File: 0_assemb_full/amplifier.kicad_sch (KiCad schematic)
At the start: 4 parts

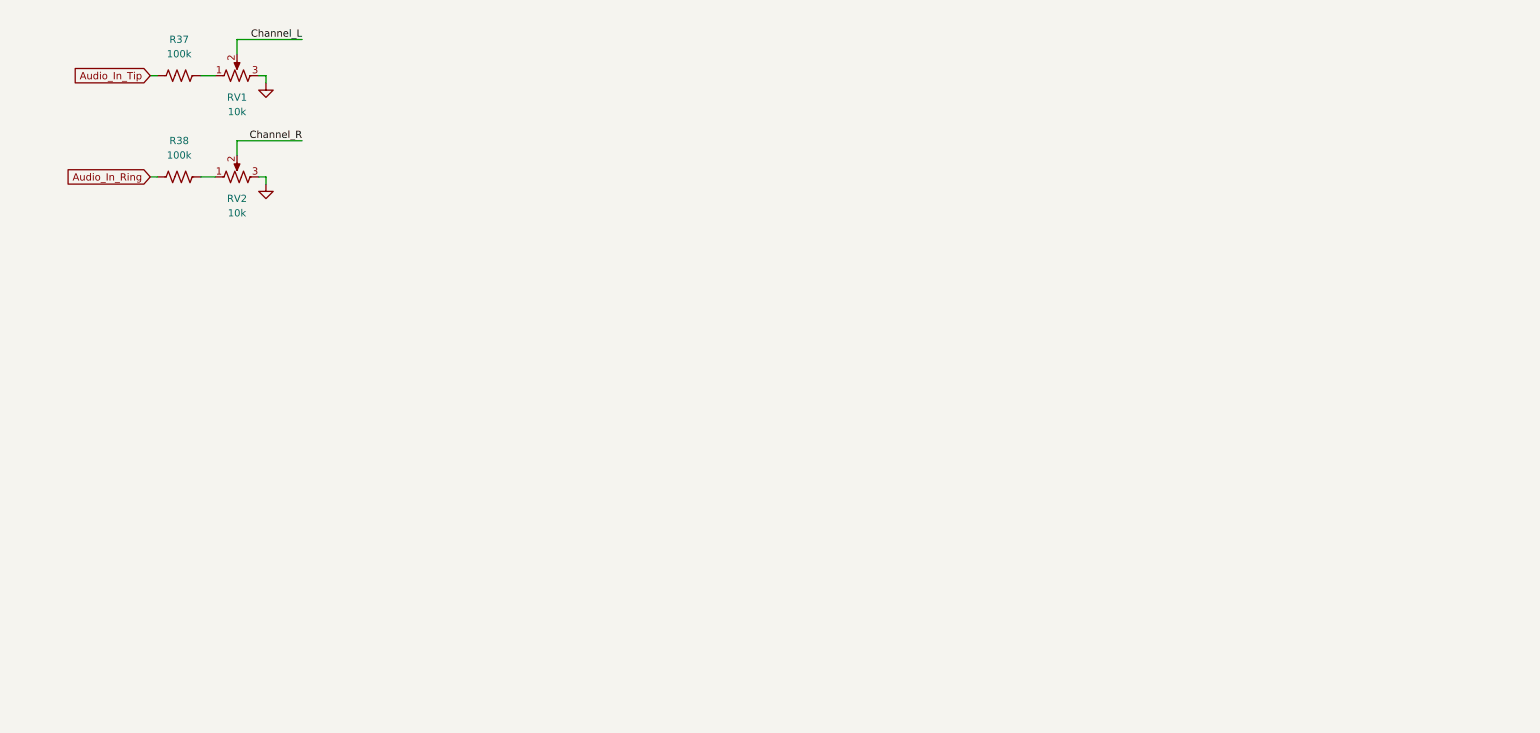
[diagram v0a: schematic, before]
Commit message: Added amplifier circuit and the programming header.
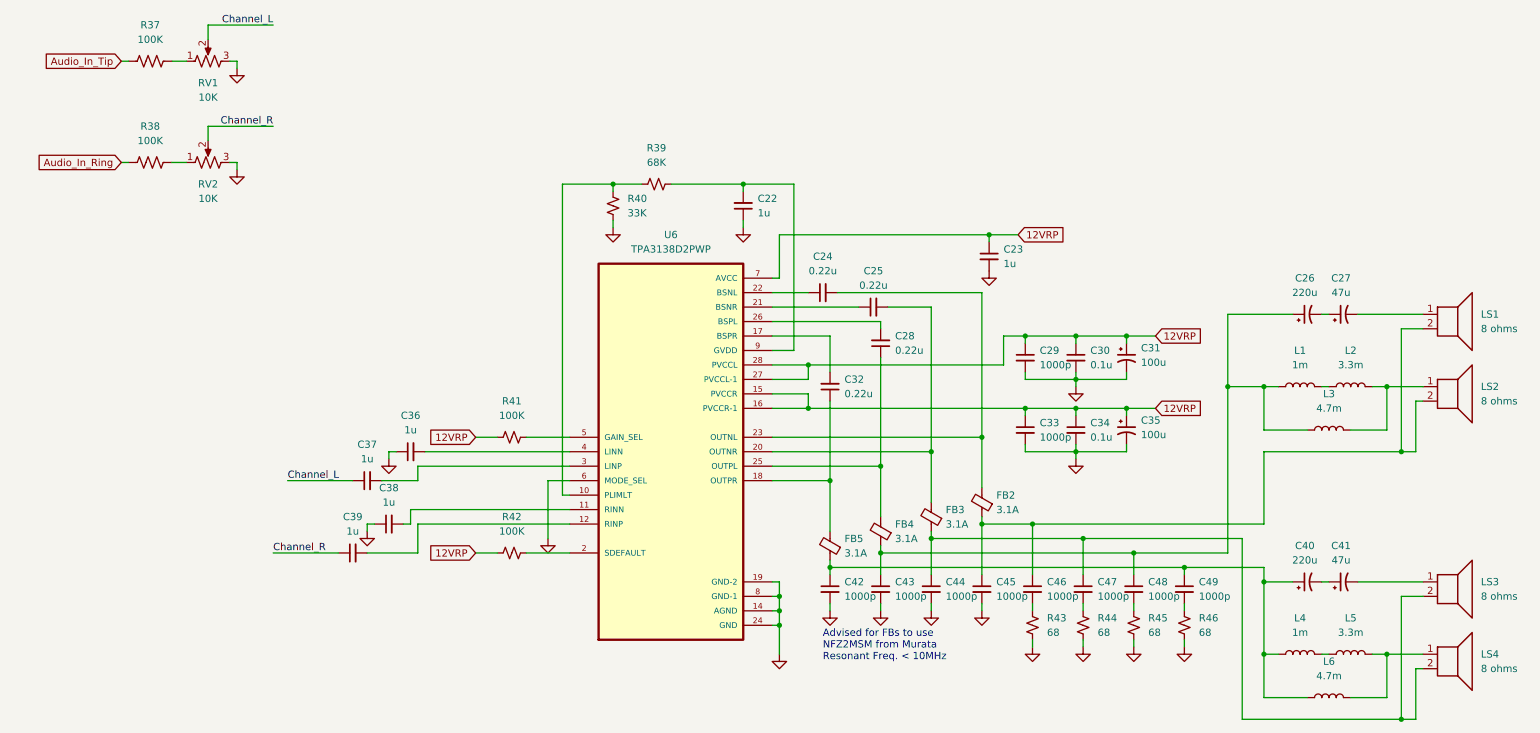
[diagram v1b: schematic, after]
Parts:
- added C22, C23, C36, C37, C38, C39: 1u, symbol Device:C_Small
- added C24, C25, C28, C32: 0.22u, symbol Device:C_Small
- added C26, C40: 220u, symbol Device:C_Polarized_Small_US
- added C27, C41: 47u, symbol Device:C_Polarized_Small_US
- added C29, C33, C42, C43, C44, C45, C46, C47, C48, C49: 1000p, symbol Device:C_Small
- added C30, C34: 0.1u, symbol Device:C_Small
- added C31, C35: 100u, symbol Device:C_Polarized_Small_US
- added FB2, FB3, FB4, FB5: 3.1A, symbol Device:FerriteBead_Small
- added L1, L4: 1m, symbol Device:L
- added L2, L5: 3.3m, symbol Device:L
- added L3, L6: 4.7m, symbol Device:L
- added LS1, LS2, LS3, LS4: 8 ohms, symbol Device:Speaker
- added R39: 68K, symbol Device:R_Small_US
- added R40: 33K, symbol Device:R_Small_US
- added R41, R42: 100K, symbol Device:R_Small_US
- added R43, R44, R45, R46: 68, symbol Device:R_Small_US
- added U6: TPA3138D2PWP, TPA3138D2PWP:IC_TPS61196PWPRQ1, symbol Specifics:TPA3138D2PWP
- R37, R38: value 100k -> 100K
- RV1, RV2: value 10k -> 10K
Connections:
- net Channel_L: now also C37.1
- net Channel_R: now also C39.1
- net GND: now also C22.1, C23.2, C29.2, C30.2, C31.2, C33.2, C34.2, C35.2, C36.1, C38.1, C42.2, C43.2, C44.2, C45.2, R40.1, R43.1, R44.1, R45.1, R46.1, U6.14 (AGND), U6.19 (GND-2), U6.24 (GND), U6.6 (MODE_SEL), U6.8 (GND-1)
- new net: R41.2, U6.5 (GAIN_SEL)
- new net: C26.1, C43.1, C48.1, FB4.1, L1.1, L3.1
- new net: L1.2, L2.1
- new net: L5.2, L6.2, LS4.1
- new net: C44.1, C47.1, FB3.1, LS3.2, LS4.2
- new net: C49.2, R46.2
- new net: C24.1, U6.22 (BSNL)
- new net: C24.2, FB2.2, U6.23 (OUTNL)
- new net: C26.2, C27.1
- new net: C27.2, LS1.1
- new net: R39.1, R40.2, U6.10 (PLIMLT)
- new net: C45.1, C46.1, FB2.1, LS1.2, LS2.2
- new net: C32.1, FB5.2, U6.18 (OUTPR)
- new net: C32.2, U6.17 (BSPR)
- new net: C46.2, R43.2
- new net: L2.2, L3.2, LS2.1
- new net: C47.2, R44.2
- new net: C28.1, FB4.2, U6.25 (OUTPL)
- new net: C36.2, U6.4 (LINN)
- new net: C38.2, U6.11 (RINN)
- new net: C25.2, FB3.2, U6.20 (OUTNR)
- new net: C40.1, C42.1, C49.1, FB5.1, L4.1, L6.1
- new net: C40.2, C41.1
- new net: C28.2, U6.26 (BSPL)
- new net: C37.2, U6.3 (LINP)
- new net: C48.2, R45.2
- new net: C41.2, LS3.1
- new net: C39.2, U6.12 (RINP)
- new net: R42.2, U6.2 (SDEFAULT)
- new net: C25.1, U6.21 (BSNR)
- new net: C22.2, R39.2, U6.9 (GVDD)
- new net: L4.2, L5.1
- new net 12VRP: C23.1, C29.1, C30.1, C31.1, C33.1, C34.1, C35.1, R41.1, R42.1, U6.15 (PVCCR), U6.16 (PVCCR-1), U6.27 (PVCCL-1), U6.28 (PVCCL), U6.7 (AVCC)
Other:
- note added: "Advised for FBs to use NFZ2MSM from Murata Resonant Freq. < 10MHz"
- moved on the sheet: R37, R38, RV1, RV2

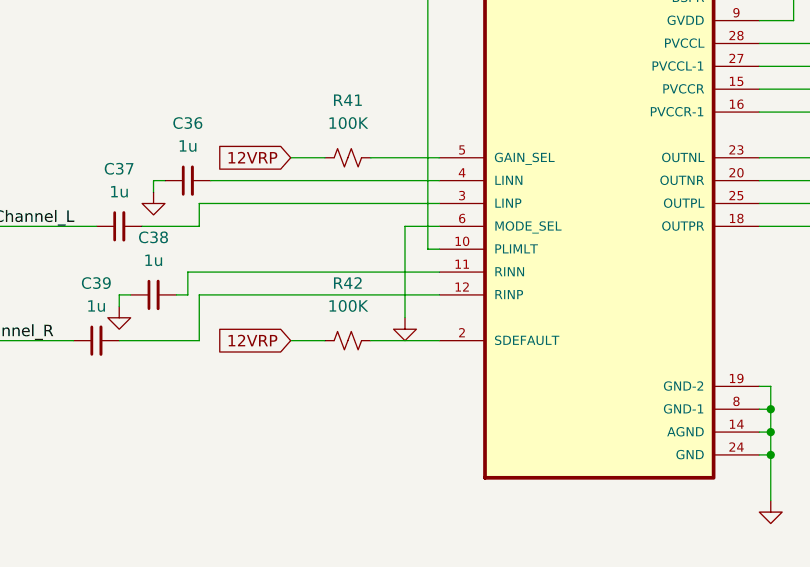
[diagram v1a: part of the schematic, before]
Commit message: A lot of work done on the STM32 PCB layout.
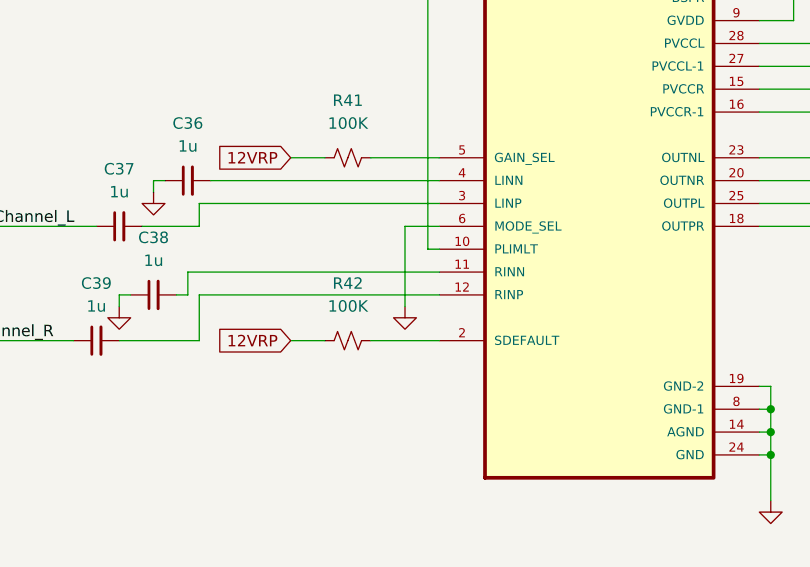
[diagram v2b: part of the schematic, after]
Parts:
- C22, C23, C31, C35, C36, C37, C38, C39: footprint (none) -> Capacitor_THT:CP_Radial_D5.0mm_P2.50mm
- C24, C25, C28, C29, C30, C32, C33, C34, C42, C43, C44, C45, C46, C47, C48, C49: footprint (none) -> Capacitor_SMD:C_0805_2012Metric_Pad1.18x1.45mm_HandSolder
- C26, C27, C40, C41: footprint (none) -> Capacitor_THT:CP_Radial_D6.3mm_P2.50mm
- FB2, FB3, FB4, FB5: footprint (none) -> Specifics:BEADC2016X100N
- L1, L2, L3, L4, L5, L6: footprint (none) -> Inductor_THT:L_Radial_D9.5mm_P5.00mm_Fastron_07HVP
- LS1, LS2, LS3, LS4: footprint (none) -> Connector_Wire:SolderWire-2.5sqmm_1x02_P7.2mm_D2.4mm_OD3.6mm
- R37, R38, R39, R40, R41, R42, R43, R44, R45, R46: footprint (none) -> Resistor_SMD:R_0805_2012Metric_Pad1.20x1.40mm_HandSolder
- RV1, RV2: footprint (none) -> Potentiometer_THT:Potentiometer_Vishay_148-149_Single_Vertical
- U6: footprint TPA3138D2PWP:IC_TPS61196PWPRQ1 -> Specifics:IC_TPS61196PWPRQ1

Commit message: Additional changes
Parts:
- C22, C23, C36, C37, C38, C39: footprint Capacitor_THT:CP_Radial_D5.0mm_P2.50mm -> Capacitor_SMD:C_0805_2012Metric_Pad1.18x1.45mm_HandSolder
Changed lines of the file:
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@@
     (property "Reference" "C36" (id 0) (at 81.2863 85.09 90))
     (property "Value" "1u" (id 1) (at 81.2863 87.63 90))
-    (property "Footprint" "Capacitor_THT:CP_Radial_D5.0mm_P2.50mm" (id 2) (at 81.28 91.44 0)
+    (property "Footprint" "Capacitor_SMD:C_0805_2012Metric_Pad1.18x1.45mm_HandSolder" (id 2) (at 81.28 91.44 0)
       (effects (font (size 1.27 1.27)) hide)
     )
@@
     (property "Reference" "C38" (id 0) (at 77.4763 97.79 90))
     (property "Value" "1u" (id 1) (at 77.4763 100.33 90))
-    (property "Footprint" "Capacitor_THT:CP_Radial_D5.0mm_P2.50mm" (id 2) (at 77.47 104.14 0)
+    (property "Footprint" "Capacitor_SMD:C_0805_2012Metric_Pad1.18x1.45mm_HandSolder" (id 2) (at 77.47 104.14 0)
       (effects (font (size 1.27 1.27)) hide)
     )
@@
     (property "Reference" "C37" (id 0) (at 73.6663 90.17 90))
     (property "Value" "1u" (id 1) (at 73.6663 92.71 90))
-    (property "Footprint" "Capacitor_THT:CP_Radial_D5.0mm_P2.50mm" (id 2) (at 73.66 96.52 0)
+    (property "Footprint" "Capacitor_SMD:C_0805_2012Metric_Pad1.18x1.45mm_HandSolder" (id 2) (at 73.66 96.52 0)
       (effects (font (size 1.27 1.27)) hide)
     )
@@
     (property "Reference" "C39" (id 0) (at 71.1263 102.87 90))
     (property "Value" "1u" (id 1) (at 71.1263 105.41 90))
-    (property "Footprint" "Capacitor_THT:CP_Radial_D5.0mm_P2.50mm" (id 2) (at 71.12 109.22 0)
+    (property "Footprint" "Capacitor_SMD:C_0805_2012Metric_Pad1.18x1.45mm_HandSolder" (id 2) (at 71.12 109.22 0)
       (effects (font (size 1.27 1.27)) hide)
     )
@@
       (effects (font (size 1.27 1.27)) (justify left))
     )
-    (property "Footprint" "Capacitor_THT:CP_Radial_D5.0mm_P2.50mm" (id 2) (at 182.88 57.15 0)
+    (property "Footprint" "Capacitor_SMD:C_0805_2012Metric_Pad1.18x1.45mm_HandSolder" (id 2) (at 182.88 57.15 0)
       (effects (font (size 1.27 1.27)) hide)
     )
@@
       (effects (font (size 1.27 1.27)) (justify right))
     )
-    (property "Footprint" "Capacitor_THT:CP_Radial_D5.0mm_P2.50mm" (id 2) (at 139.7 48.26 0)
-      (effects (font (size 1.27 1.27)) hide)
-    )
+    (property "Footprint" "Capacitor_SMD:C_0805_2012Metric_Pad1.18x1.45mm_HandSolder" (id 2) (at 139.7 48.26 0)
+      (effects (font (size 1.27 1.27)) hide)
+    )

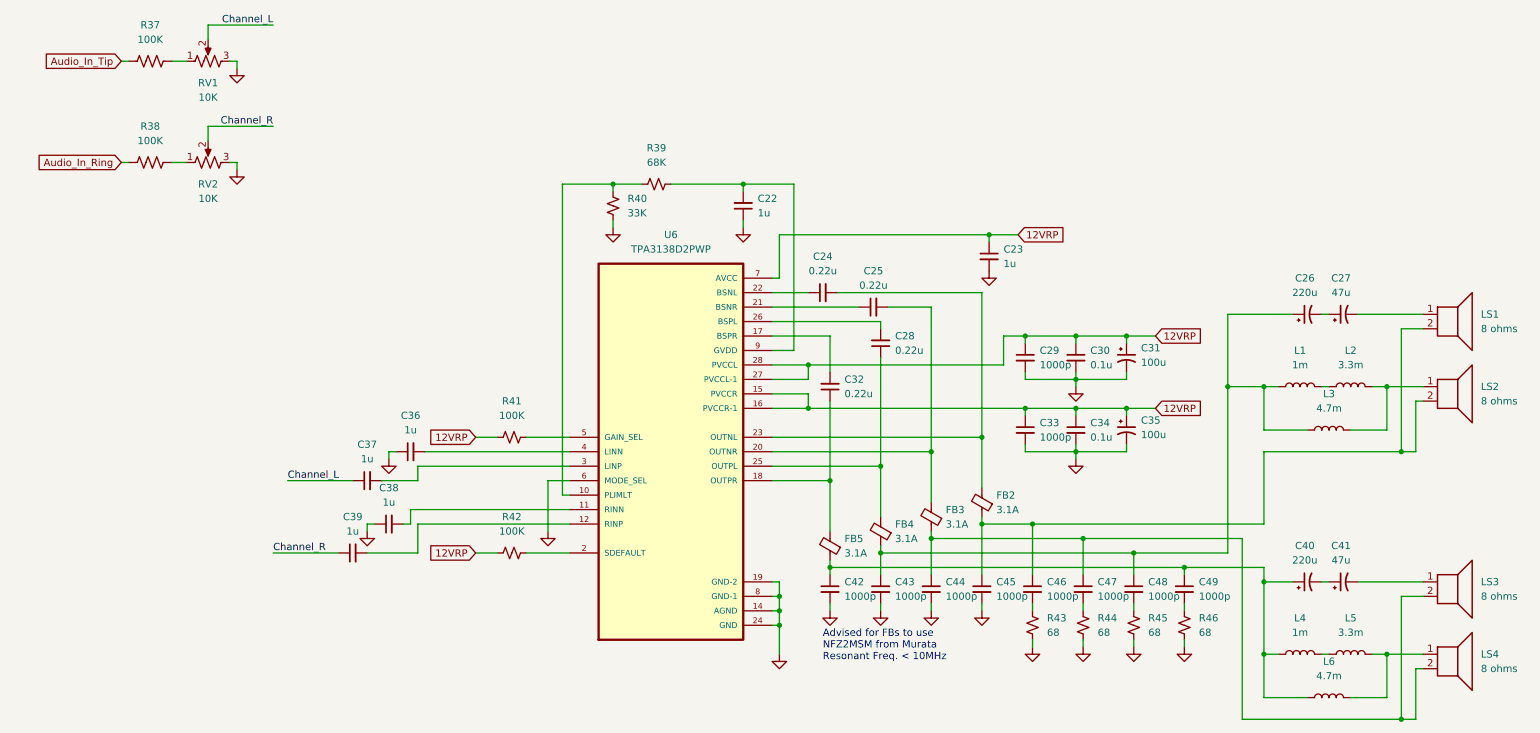
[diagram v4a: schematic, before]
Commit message: Active Filters layout added
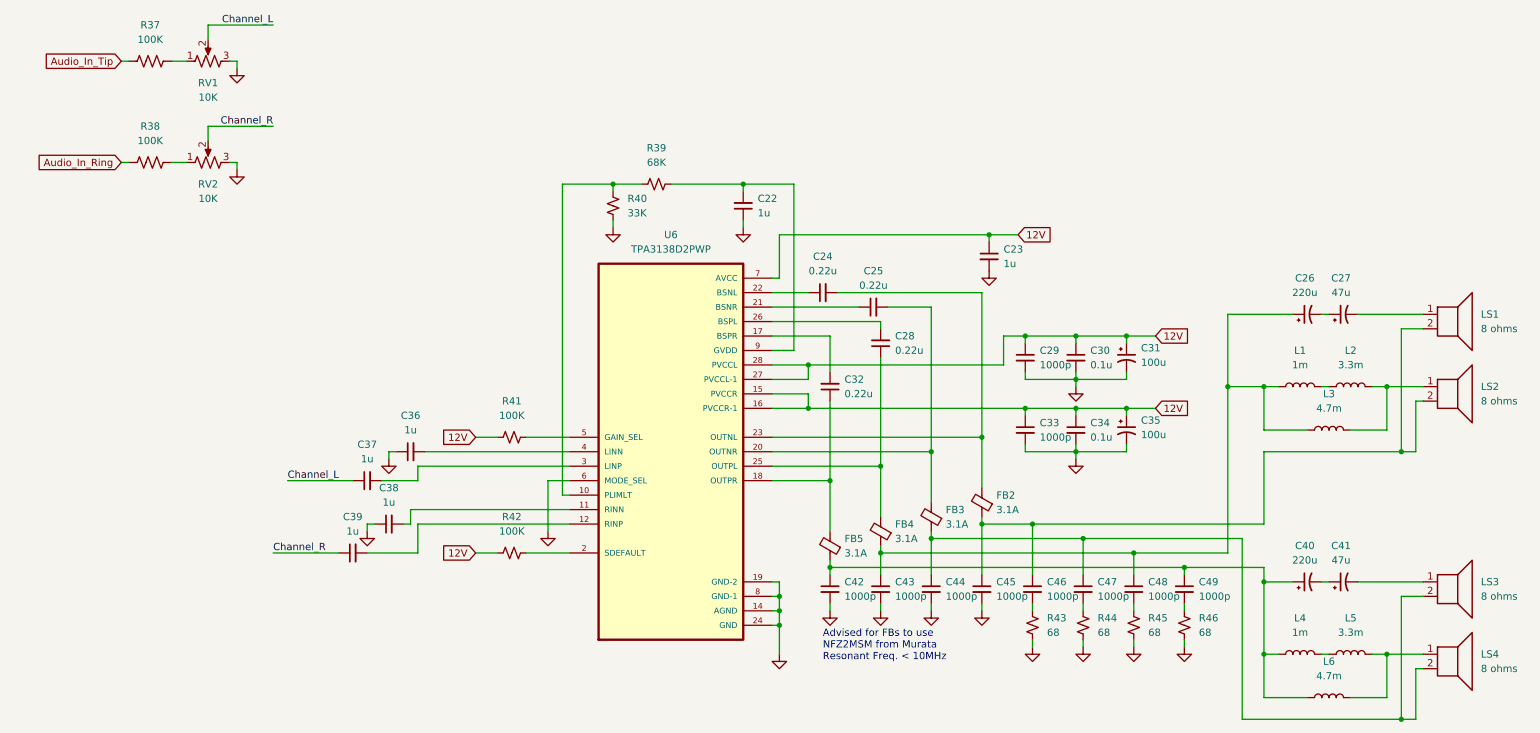
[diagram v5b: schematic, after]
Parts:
- LS1, LS2, LS3, LS4: footprint Connector_Wire:SolderWire-2.5sqmm_1x02_P7.2mm_D2.4mm_OD3.6mm -> Connector_Wire:SolderWire-2sqmm_1x02_P7.8mm_D2mm_OD3.9mm
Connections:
- net 12VRP renamed 12V
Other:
- title: (none) -> Class-D Amplifier
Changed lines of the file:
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@@
 (kicad_sch (version 20211123) (generator eeschema)
   (paper "A4")
+  (title_block
+    (title "Class-D Amplifier")
+  )
   (junction (at 231.14 114.3) (diameter 0) (color 0 0 0 0)
   )
@@
     )
   )
-  (global_label "12VRP" (shape input) (at 92.71 88.9 180) (fields_autoplaced)
+  (global_label "12V" (shape input) (at 92.71 88.9 180) (fields_autoplaced)
     (effects (font (size 1.27 1.27)) (justify right))
-    (property "Intersheet References" "${INTERSHEET_REFS}" (id 0) (at 84.2493 88.8206 0)
+    (property "Intersheet References" "${INTERSHEET_REFS}" (id 0) (at 86.7893 88.8206 0)
       (effects (font (size 1.27 1.27)) (justify right) hide)
     )
   )
-  (global_label "12VRP" (shape input) (at 212.09 83.82 0) (fields_autoplaced)
+  (global_label "12V" (shape input) (at 212.09 83.82 0) (fields_autoplaced)
     (effects (font (size 1.27 1.27)) (justify left))
-    (property "Intersheet References" "${INTERSHEET_REFS}" (id 0) (at 220.5507 83.8994 0)
+    (property "Intersheet References" "${INTERSHEET_REFS}" (id 0) (at 218.0107 83.7406 0)
       (effects (font (size 1.27 1.27)) (justify left) hide)
     )
   )
-  (global_label "12VRP" (shape input) (at 92.71 109.22 180) (fields_autoplaced)
+  (global_label "12V" (shape input) (at 92.71 109.22 180) (fields_autoplaced)
     (effects (font (size 1.27 1.27)) (justify right))
-    (property "Intersheet References" "${INTERSHEET_REFS}" (id 0) (at 84.2493 109.1406 0)
+    (property "Intersheet References" "${INTERSHEET_REFS}" (id 0) (at 86.7893 109.1406 0)
       (effects (font (size 1.27 1.27)) (justify right) hide)
     )
   )
-  (global_label "12VRP" (shape input) (at 212.09 71.12 0) (fields_autoplaced)
+  (global_label "12V" (shape input) (at 212.09 71.12 0) (fields_autoplaced)
     (effects (font (size 1.27 1.27)) (justify left))
-    (property "Intersheet References" "${INTERSHEET_REFS}" (id 0) (at 220.5507 71.1994 0)
+    (property "Intersheet References" "${INTERSHEET_REFS}" (id 0) (at 218.0107 71.0406 0)
       (effects (font (size 1.27 1.27)) (justify left) hide)
     )
   )
-  (global_label "12VRP" (shape input) (at 187.96 53.34 0) (fields_autoplaced)
+  (global_label "12V" (shape input) (at 187.96 53.34 0) (fields_autoplaced)
     (effects (font (size 1.27 1.27)) (justify left))
-    (property "Intersheet References" "${INTERSHEET_REFS}" (id 0) (at 196.4207 53.4194 0)
+    (property "Intersheet References" "${INTERSHEET_REFS}" (id 0) (at 193.8807 53.2606 0)
       (effects (font (size 1.27 1.27)) (justify left) hide)
     )
@@
       (effects (font (size 1.27 1.27)) (justify left))
     )
-    (property "Footprint" "Connector_Wire:SolderWire-2.5sqmm_1x02_P7.2mm_D2.4mm_OD3.6mm" (id 2) (at 264.16 132.08 0)
+    (property "Footprint" "Connector_Wire:SolderWire-2sqmm_1x02_P7.8mm_D2mm_OD3.9mm" (id 2) (at 264.16 132.08 0)
       (effects (font (size 1.27 1.27)) hide)
     )
@@
       (effects (font (size 1.27 1.27)) (justify left))
     )
-    (property "Footprint" "Connector_Wire:SolderWire-2.5sqmm_1x02_P7.2mm_D2.4mm_OD3.6mm" (id 2) (at 264.16 72.39 0)
+    (property "Footprint" "Connector_Wire:SolderWire-2sqmm_1x02_P7.8mm_D2mm_OD3.9mm" (id 2) (at 264.16 72.39 0)
       (effects (font (size 1.27 1.27)) hide)
     )
@@
       (effects (font (size 1.27 1.27)) (justify left))
     )
-    (property "Footprint" "Connector_Wire:SolderWire-2.5sqmm_1x02_P7.2mm_D2.4mm_OD3.6mm" (id 2) (at 264.16 85.09 0)
+    (property "Footprint" "Connector_Wire:SolderWire-2sqmm_1x02_P7.8mm_D2mm_OD3.9mm" (id 2) (at 264.16 85.09 0)
       (effects (font (size 1.27 1.27)) hide)
     )
@@
       (effects (font (size 1.27 1.27)) (justify left))
     )
-    (property "Footprint" "Connector_Wire:SolderWire-2.5sqmm_1x02_P7.2mm_D2.4mm_OD3.6mm" (id 2) (at 264.16 119.38 0)
-      (effects (font (size 1.27 1.27)) hide)
-    )
+    (property "Footprint" "Connector_Wire:SolderWire-2sqmm_1x02_P7.8mm_D2mm_OD3.9mm" (id 2) (at 264.16 119.38 0)
+      (effects (font (size 1.27 1.27)) hide)
+    )
